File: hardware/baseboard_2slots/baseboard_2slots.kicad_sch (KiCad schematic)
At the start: 43 parts, among them J1 IO-Board_00, J10 Conn_01x04_Male, J11 Conn_01x04_Male, J12 Conn_01x04_Male, J13 Conn_01x04_Male, J14 Conn_01x04_Male, J15 Conn_02x02_Odd_Even, J2 IO-Board_01, J5 USB_B_Micro, J6 Conn_01x05: Adafruit 1833, J7 Screw_Terminal_01x04, J8 Conn_02x02_Odd_Even, J9 Conn_02x02_Odd_Even, U1 NRF24L01_Breakout, U2 Pico, U3 W5500_Mini

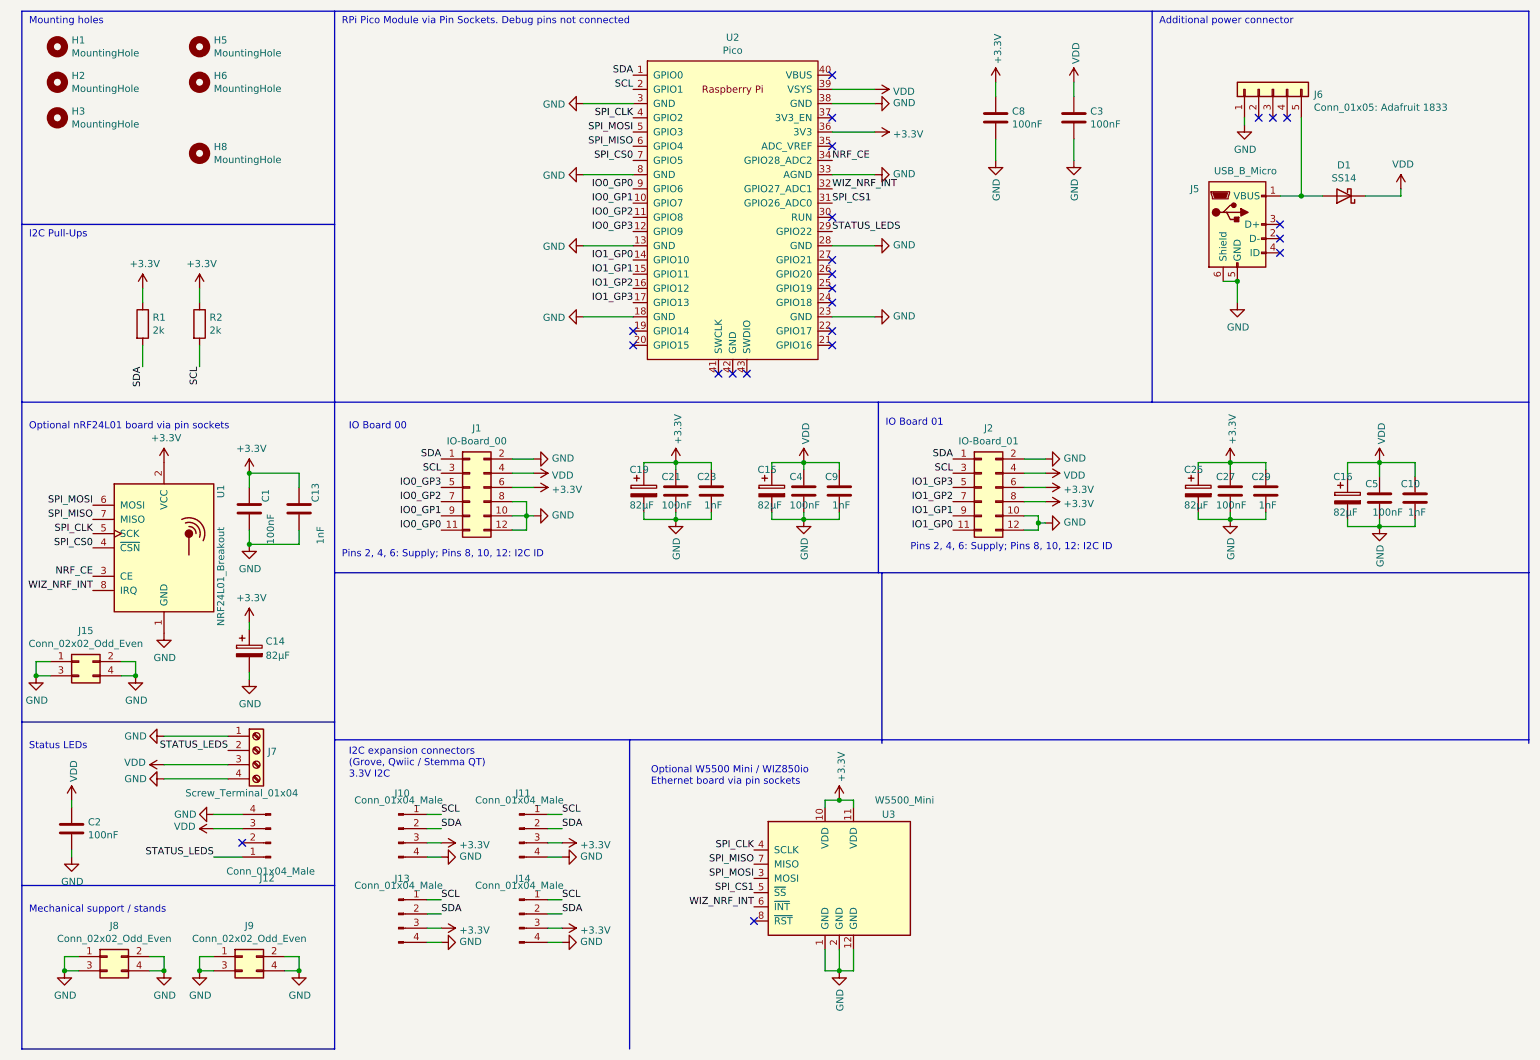
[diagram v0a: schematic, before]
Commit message: Add a IRQ config jumper for the nRF24 and the Wiz modules
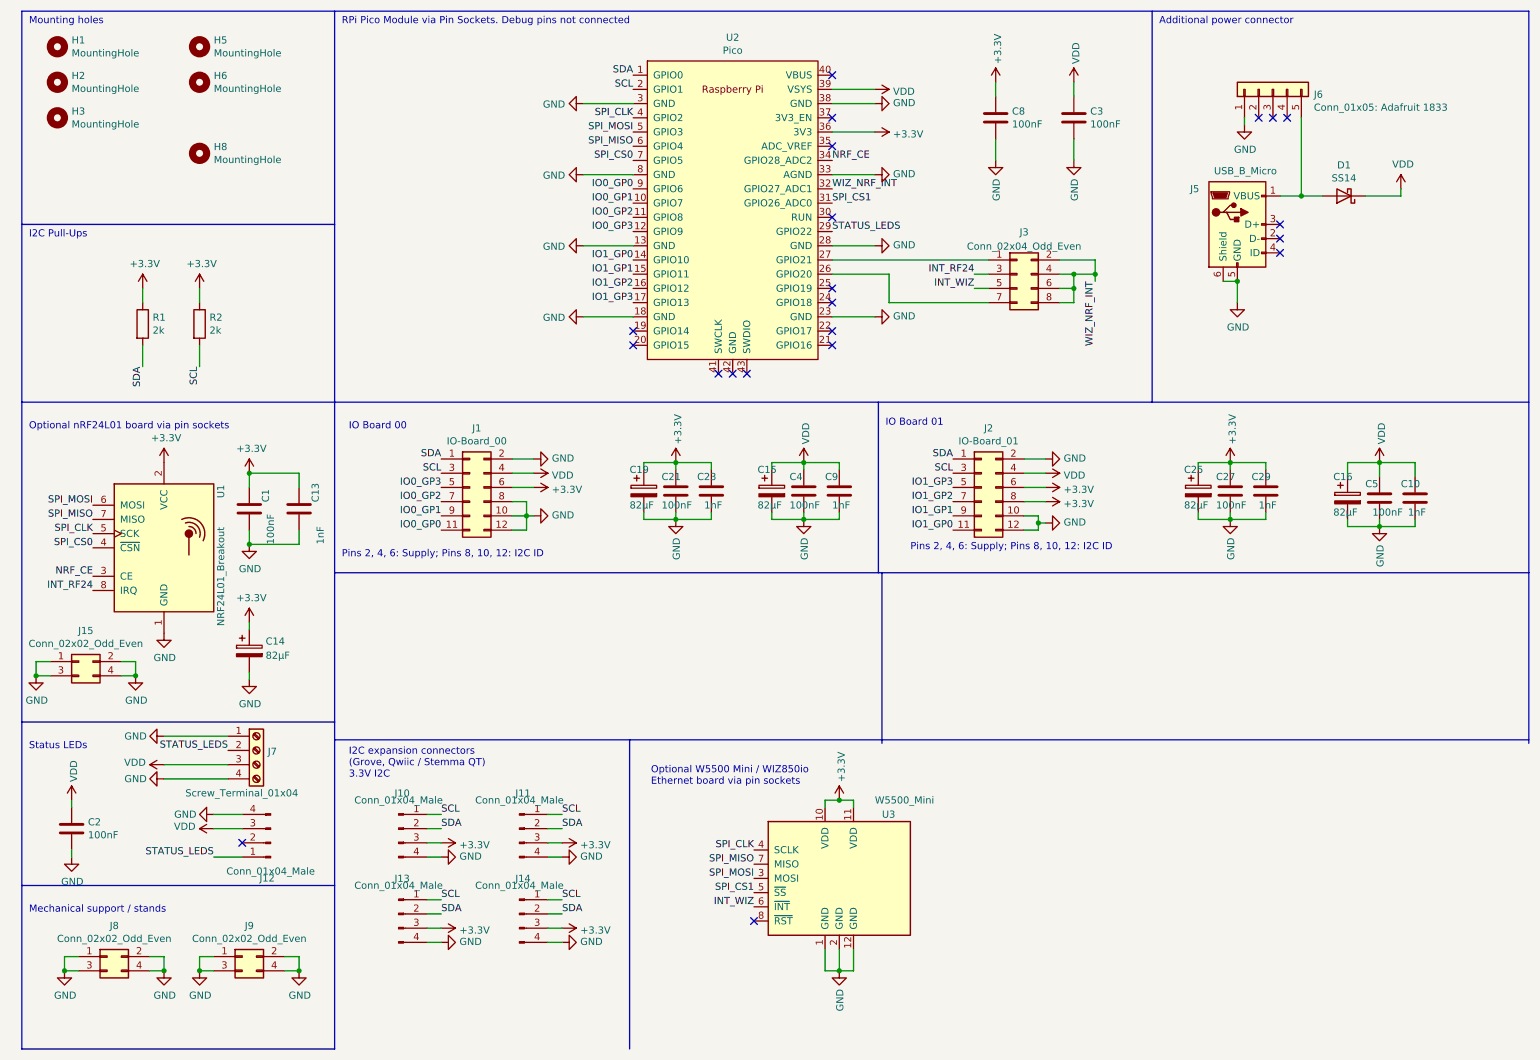
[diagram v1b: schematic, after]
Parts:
- added J3: Conn_02x04_Odd_Even, Connector_PinHeader_2.54mm:PinHeader_2x04_P2.54mm_Vertical, symbol Connector_Generic:Conn_02x04_Odd_Even
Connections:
- net WIZ_NRF_INT: now also J3.2 (Pin_2), J3.4 (Pin_4), J3.6 (Pin_6), J3.8 (Pin_8); no longer U1.8 (IRQ), U3.6 (~{INT})
- net at U2.26 (GPIO20): now also J3.7 (Pin_7)
- net at U2.27 (GPIO21): now also J3.1 (Pin_1)
- new net INT_RF24: J3.3 (Pin_3), U1.8 (IRQ)
- new net INT_WIZ: J3.5 (Pin_5), U3.6 (~{INT})
- no-connect marks 23 -> 21
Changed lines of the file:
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@@
   (junction (at 241.3 45.72) (diameter 0) (color 0 0 0 0)
   )
+  (junction (at 200.66 59.69) (diameter 0) (color 0 0 0 0)
+  )
   (junction (at 38.1 184.15) (diameter 0) (color 0 0 0 0)
   )
@@
   (junction (at 62.23 184.15) (diameter 0) (color 0 0 0 0)
   )
+  (junction (at 204.47 59.69) (diameter 0) (color 0 0 0 0)
+  )
   (junction (at 255.27 93.345) (diameter 0) (color 0 0 0 0)
   )
@@
   )
   (junction (at 15.24 131.445) (diameter 0) (color 0 0 0 0)
+  )
+  (junction (at 200.66 62.23) (diameter 0) (color 0 0 0 0)
   )
   (no_connect (at 237.49 55.88))
@@
   (no_connect (at 157.48 36.83))
   (no_connect (at 121.92 69.85))
-  (no_connect (at 157.48 59.69))
   (no_connect (at 52.07 161.29))
   (no_connect (at 157.48 72.39))
@@
   (no_connect (at 233.68 31.75))
   (no_connect (at 142.24 77.47))
-  (no_connect (at 157.48 57.15))
   (no_connect (at 238.76 31.75))
   (no_connect (at 236.22 31.75))
@@
     (stroke (width 0) (type default) (color 0 0 0 0))
   )
+  (wire (pts (xy 182.88 62.23) (xy 185.42 62.23))
+    (stroke (width 0) (type default) (color 0 0 0 0))
+  )
   (polyline (pts (xy 68.58 198.12) (xy 12.7 198.12))
     (stroke (width 0) (type default) (color 0 0 0 0))
@@
     (stroke (width 0) (type default) (color 0 0 0 0))
   )
+  (wire (pts (xy 182.88 59.69) (xy 185.42 59.69))
+    (stroke (width 0) (type default) (color 0 0 0 0))
+  )
   (wire (pts (xy 228.6 93.345) (xy 234.95 93.345))
     (stroke (width 0) (type default) (color 0 0 0 0))
@@
     (stroke (width 0) (type default) (color 0 0 0 0))
   )
+  (wire (pts (xy 157.48 57.15) (xy 185.42 57.15))
+    (stroke (width 0) (type default) (color 0 0 0 0))
+  )
   (wire (pts (xy 191.77 95.25) (xy 195.58 95.25))
     (stroke (width 0) (type default) (color 0 0 0 0))
@@
     (stroke (width 0) (type default) (color 0 0 0 0))
   )
+  (wire (pts (xy 204.47 57.15) (xy 204.47 59.69))
+    (stroke (width 0) (type default) (color 0 0 0 0))
+  )
   (wire (pts (xy 106.68 173.99) (xy 109.22 173.99))
     (stroke (width 0) (type default) (color 0 0 0 0))
@@
     (stroke (width 0) (type default) (color 0 0 0 0))
   )
+  (wire (pts (xy 167.64 59.69) (xy 167.64 64.77))
+    (stroke (width 0) (type default) (color 0 0 0 0))
+  )
   (polyline (pts (xy 281.94 113.03) (xy 281.94 143.51))
     (stroke (width 0) (type default) (color 0 0 0 0))
   )
+  (wire (pts (xy 200.66 64.77) (xy 200.66 62.23))
+    (stroke (width 0) (type default) (color 0 0 0 0))
+  )
   (wire (pts (xy 252.73 45.72) (xy 259.08 45.72))
     (stroke (width 0) (type default) (color 0 0 0 0))
@@
     (stroke (width 0) (type default) (color 0 0 0 0))
   )
+  (wire (pts (xy 198.12 62.23) (xy 200.66 62.23))
+    (stroke (width 0) (type default) (color 0 0 0 0))
+  )
   (wire (pts (xy 33.02 128.905) (xy 33.02 131.445))
     (stroke (width 0) (type default) (color 0 0 0 0))
@@
     (stroke (width 0) (type default) (color 0 0 0 0))
   )
+  (wire (pts (xy 167.64 64.77) (xy 185.42 64.77))
+    (stroke (width 0) (type default) (color 0 0 0 0))
+  )
   (polyline (pts (xy 12.7 198.12) (xy 12.7 12.7))
     (stroke (width 0) (type default) (color 0 0 0 0))
@@
     (stroke (width 0) (type default) (color 0 0 0 0))
   )
+  (wire (pts (xy 198.12 64.77) (xy 200.66 64.77))
+    (stroke (width 0) (type default) (color 0 0 0 0))
+  )
   (wire (pts (xy 157.48 54.61) (xy 165.1 54.61))
     (stroke (width 0) (type default) (color 0 0 0 0))
@@
     (stroke (width 0) (type default) (color 0 0 0 0))
   )
+  (wire (pts (xy 198.12 59.69) (xy 200.66 59.69))
+    (stroke (width 0) (type default) (color 0 0 0 0))
+  )
   (polyline (pts (xy 12.7 82.55) (xy 281.94 82.55))
     (stroke (width 0) (type default) (color 0 0 0 0))
@@
     (stroke (width 0) (type default) (color 0 0 0 0))
   )
+  (wire (pts (xy 200.66 62.23) (xy 200.66 59.69))
+    (stroke (width 0) (type default) (color 0 0 0 0))
+  )
   (wire (pts (xy 35.56 181.61) (xy 38.1 181.61))
     (stroke (width 0) (type default) (color 0 0 0 0))
@@
     (stroke (width 0) (type default) (color 0 0 0 0))
   )
+  (wire (pts (xy 198.12 57.15) (xy 204.47 57.15))
+    (stroke (width 0) (type default) (color 0 0 0 0))
+  )
   (wire (pts (xy 106.68 161.29) (xy 109.22 161.29))
     (stroke (width 0) (type default) (color 0 0 0 0))
@@
     (stroke (width 0) (type default) (color 0 0 0 0))
   )
+  (wire (pts (xy 200.66 59.69) (xy 204.47 59.69))
+    (stroke (width 0) (type default) (color 0 0 0 0))
+  )
   (wire (pts (xy 129.54 93.345) (xy 135.89 93.345))
     (stroke (width 0) (type default) (color 0 0 0 0))
@@
     (stroke (width 0) (type default) (color 0 0 0 0))
   )
+  (wire (pts (xy 204.47 59.69) (xy 204.47 60.96))
+    (stroke (width 0) (type default) (color 0 0 0 0))
+  )
   (wire (pts (xy 191.77 100.33) (xy 195.58 100.33))
     (stroke (width 0) (type default) (color 0 0 0 0))
@@
   )
   (wire (pts (xy 255.27 104.775) (xy 261.62 104.775))
+    (stroke (width 0) (type default) (color 0 0 0 0))
+  )
+  (wire (pts (xy 157.48 59.69) (xy 167.64 59.69))
     (stroke (width 0) (type default) (color 0 0 0 0))
   )
@@
     (effects (font (size 1.27 1.27)) (justify left bottom))
   )
+  (label "INT_RF24" (at 182.88 59.69 180)
+    (effects (font (size 1.27 1.27)) (justify right bottom))
+  )
   (label "IO1_GP1" (at 121.92 59.69 180)
     (effects (font (size 1.27 1.27)) (justify right bottom))
@@
     (effects (font (size 1.27 1.27)) (justify right bottom))
   )
-  (label "WIZ_NRF_INT" (at 143.51 172.72 180)
+  (label "INT_WIZ" (at 143.51 172.72 180)
     (effects (font (size 1.27 1.27)) (justify right bottom))
   )
@@
     (effects (font (size 1.27 1.27)) (justify left bottom))
   )
+  (label "INT_WIZ" (at 182.88 62.23 180)
+    (effects (font (size 1.27 1.27)) (justify right bottom))
+  )
   (label "SCL" (at 109.22 156.21 0)
     (effects (font (size 1.27 1.27)) (justify left bottom))
@@
     (effects (font (size 1.27 1.27)) (justify right bottom))
   )
-  (label "WIZ_NRF_INT" (at 25.4 116.205 180)
+  (label "INT_RF24" (at 25.4 116.205 180)
     (effects (font (size 1.27 1.27)) (justify right bottom))
   )
@@
   )
   (label "IO0_GP0" (at 87.63 105.41 180)
+    (effects (font (size 1.27 1.27)) (justify right bottom))
+  )
+  (label "WIZ_NRF_INT" (at 204.47 60.96 270)
     (effects (font (size 1.27 1.27)) (justify right bottom))
   )
@@
     (pin "4")
   )
+  (symbol (lib_id "Connector_Generic:Conn_02x04_Odd_Even") (at 190.5 59.69 0) (unit 1)
+    (in_bom yes) (on_board yes) (fields_autoplaced)
+    (property "Reference" "J3" (id 0) (at 191.77 52.1802 0))
+    (property "Value" "Conn_02x04_Odd_Even" (id 1) (at 191.77 54.7171 0))
+    (property "Footprint" "Connector_PinHeader_2.54mm:PinHeader_2x04_P2.54mm_Vertical" (id 2) (at 190.5 59.69 0)
+      (effects (font (size 1.27 1.27)) hide)
+    )
+    (property "Datasheet" "~" (id 3) (at 190.5 59.69 0)
+      (effects (font (size 1.27 1.27)) hide)
+    )
+    (pin "1")
+    (pin "2")
+    (pin "3")
+    (pin "4")
+    (pin "5")
+    (pin "6")
+    (pin "7")
+    (pin "8")
+  )
   (symbol (lib_id "Connector:Conn_01x04_Male") (at 80.01 173.99 0) (unit 1)
     (in_bom yes) (on_board yes)
@@
       (reference "J2") (unit 1) (value "IO-Board_01") (footprint "Connector_PinSocket_2.54mm:PinSocket_2x06_P2.54mm_Vertical")
     )
+    (path "/98ccf2a9-157e-4e8e-8a65-3d0157ea5ef7"
+      (reference "J3") (unit 1) (value "Conn_02x04_Odd_Even") (footprint "Connector_PinHeader_2.54mm:PinHeader_2x04_P2.54mm_Vertical")
+    )
     (path "/00000000-0000-0000-0000-00006053037d"

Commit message: Hardware: Add missing LCSC references for some caps
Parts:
- C23, C29, C9: LCSC (none) -> C1588
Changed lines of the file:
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@@
+      (effects (font (size 1.27 1.27)) hide)
+    )
+    (property "LCSC" "C1588" (id 4) (at 158.75 98.425 0)
       (effects (font (size 1.27 1.27)) hide)
     )
@@
       (effects (font (size 1.27 1.27)) hide)
     )
+    (property "LCSC" "C1588" (id 4) (at 234.95 98.425 0)
+      (effects (font (size 1.27 1.27)) hide)
+    )
     (pin "1")
     (pin "2")
@@
       (effects (font (size 1.27 1.27)) hide)
     )
+    (property "LCSC" "C1588" (id 4) (at 135.89 98.425 0)
+      (effects (font (size 1.27 1.27)) hide)
+    )

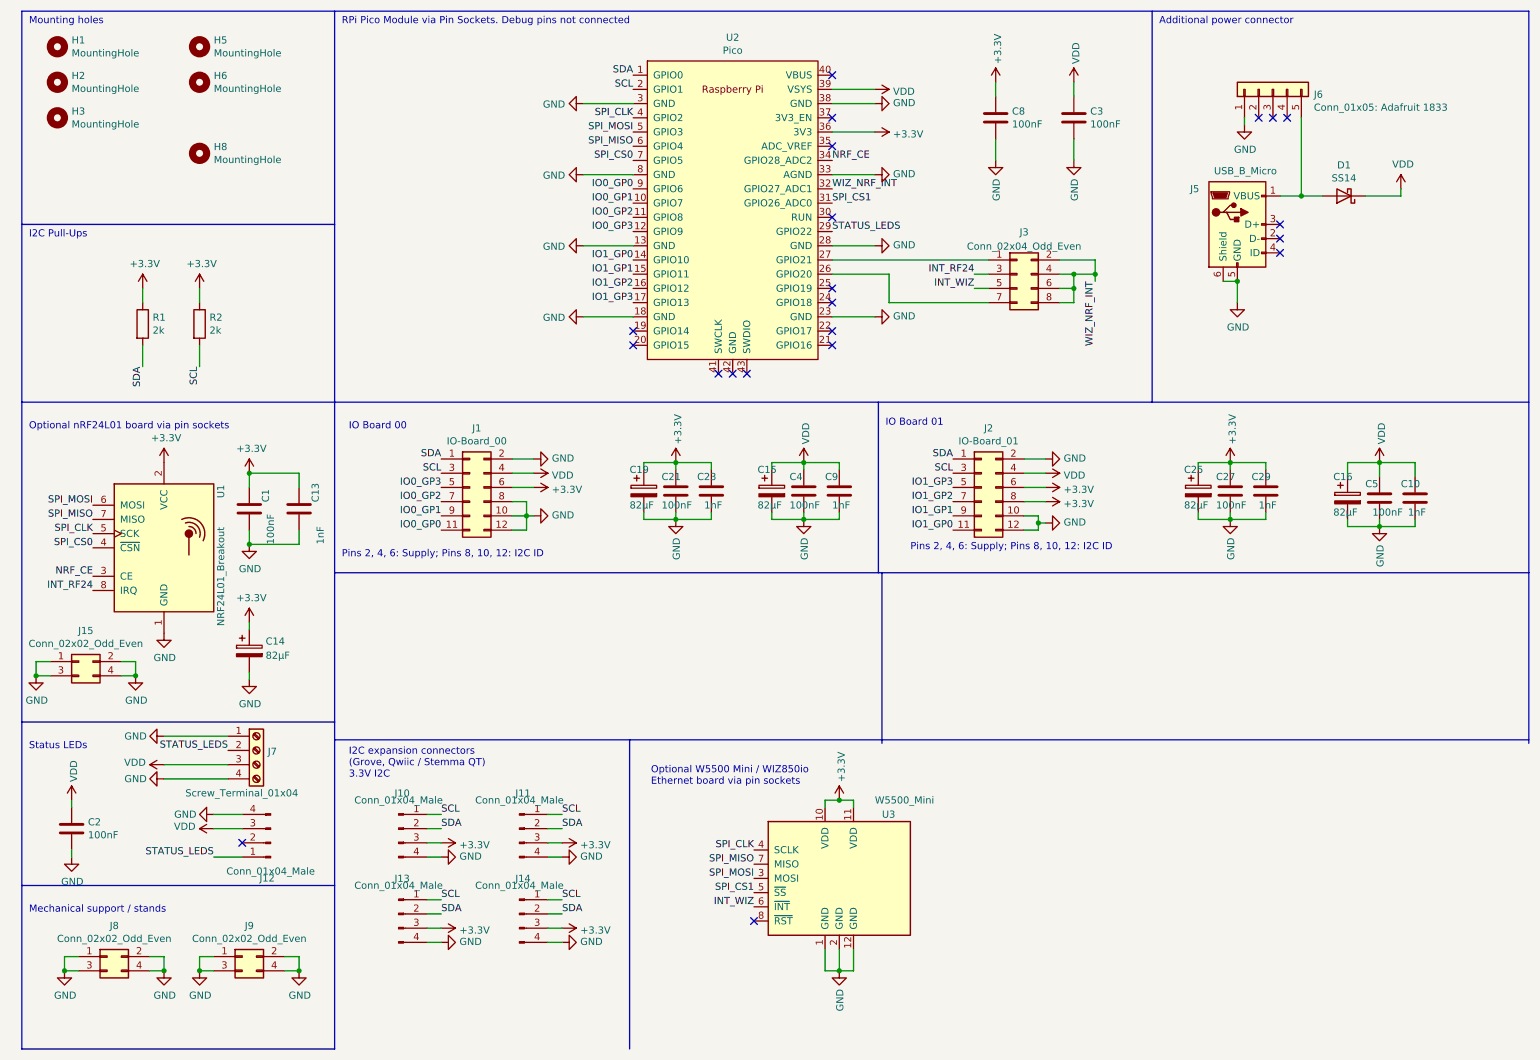
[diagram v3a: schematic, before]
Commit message: Update baseboards to KiCad 8, add copper keepout underneath Picos, add OpenHardware logo
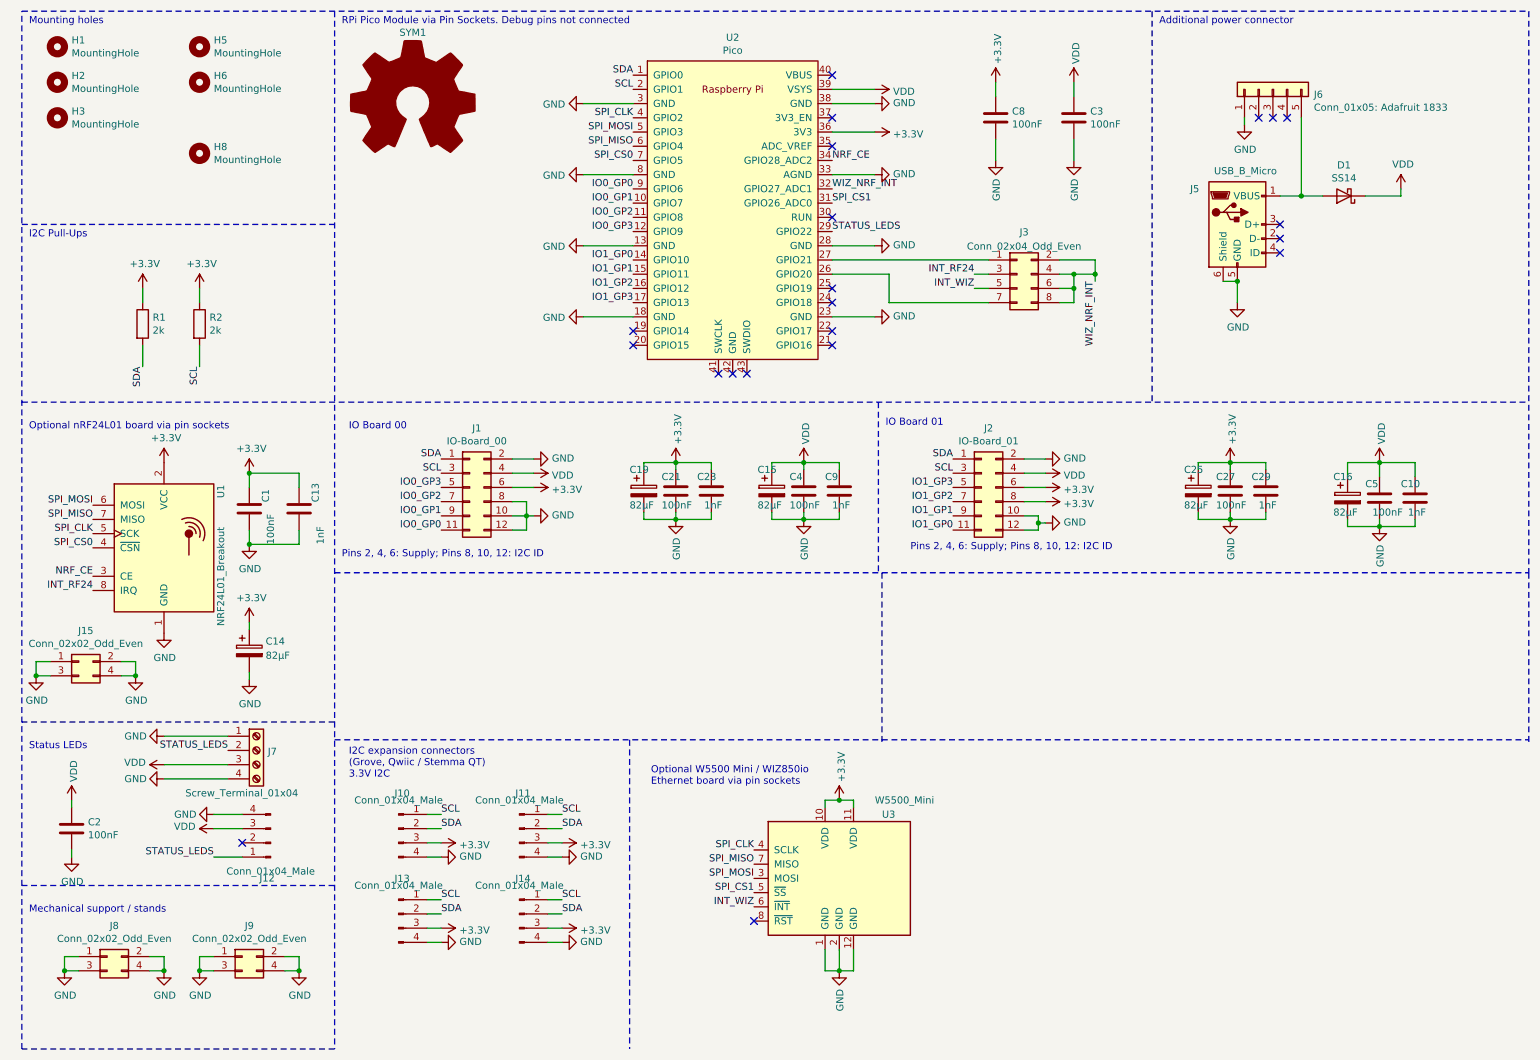
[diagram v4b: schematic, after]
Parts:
- added SYM1: Logo_Open_Hardware_Large, Symbol:OSHW-Logo2_14.6x12mm_SilkScreen, symbol Graphic:Logo_Open_Hardware_Large
